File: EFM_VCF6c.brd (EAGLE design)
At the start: 100 x 80.6 mm, 69 parts, among them IC1 LM13700N, Q1 2N3904, Q2 2N3904, Q3 2N3906, Q4 2N3904, Q5 2N3906, U1 POWER

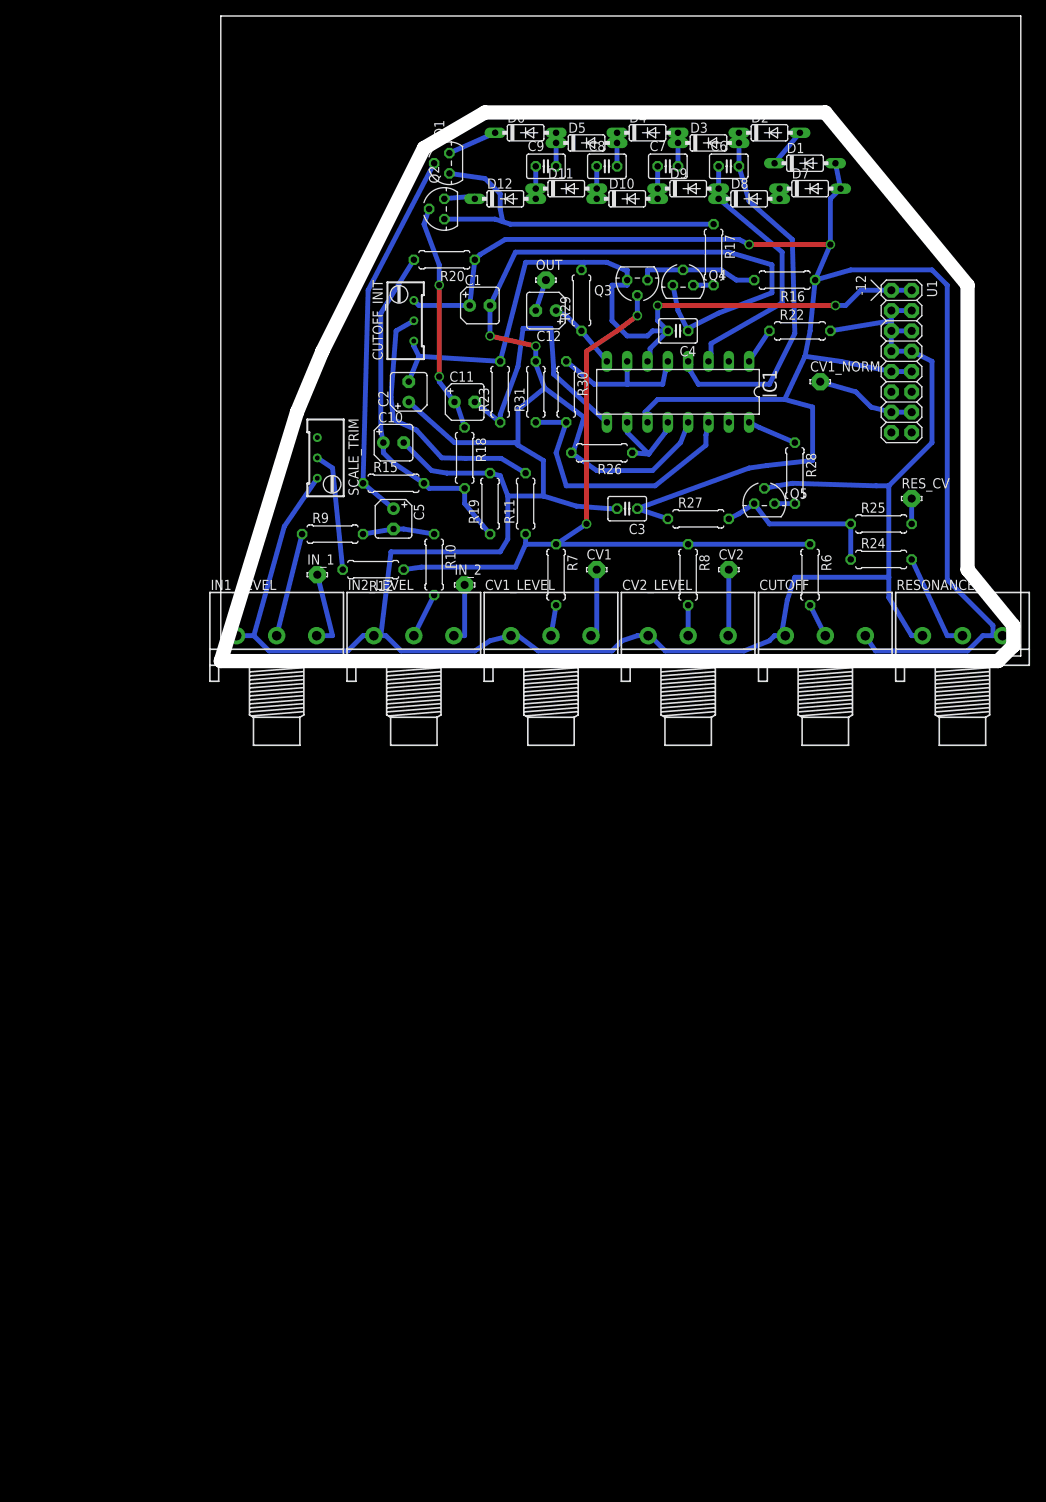
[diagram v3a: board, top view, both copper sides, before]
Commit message: updated power and pots and better diodes
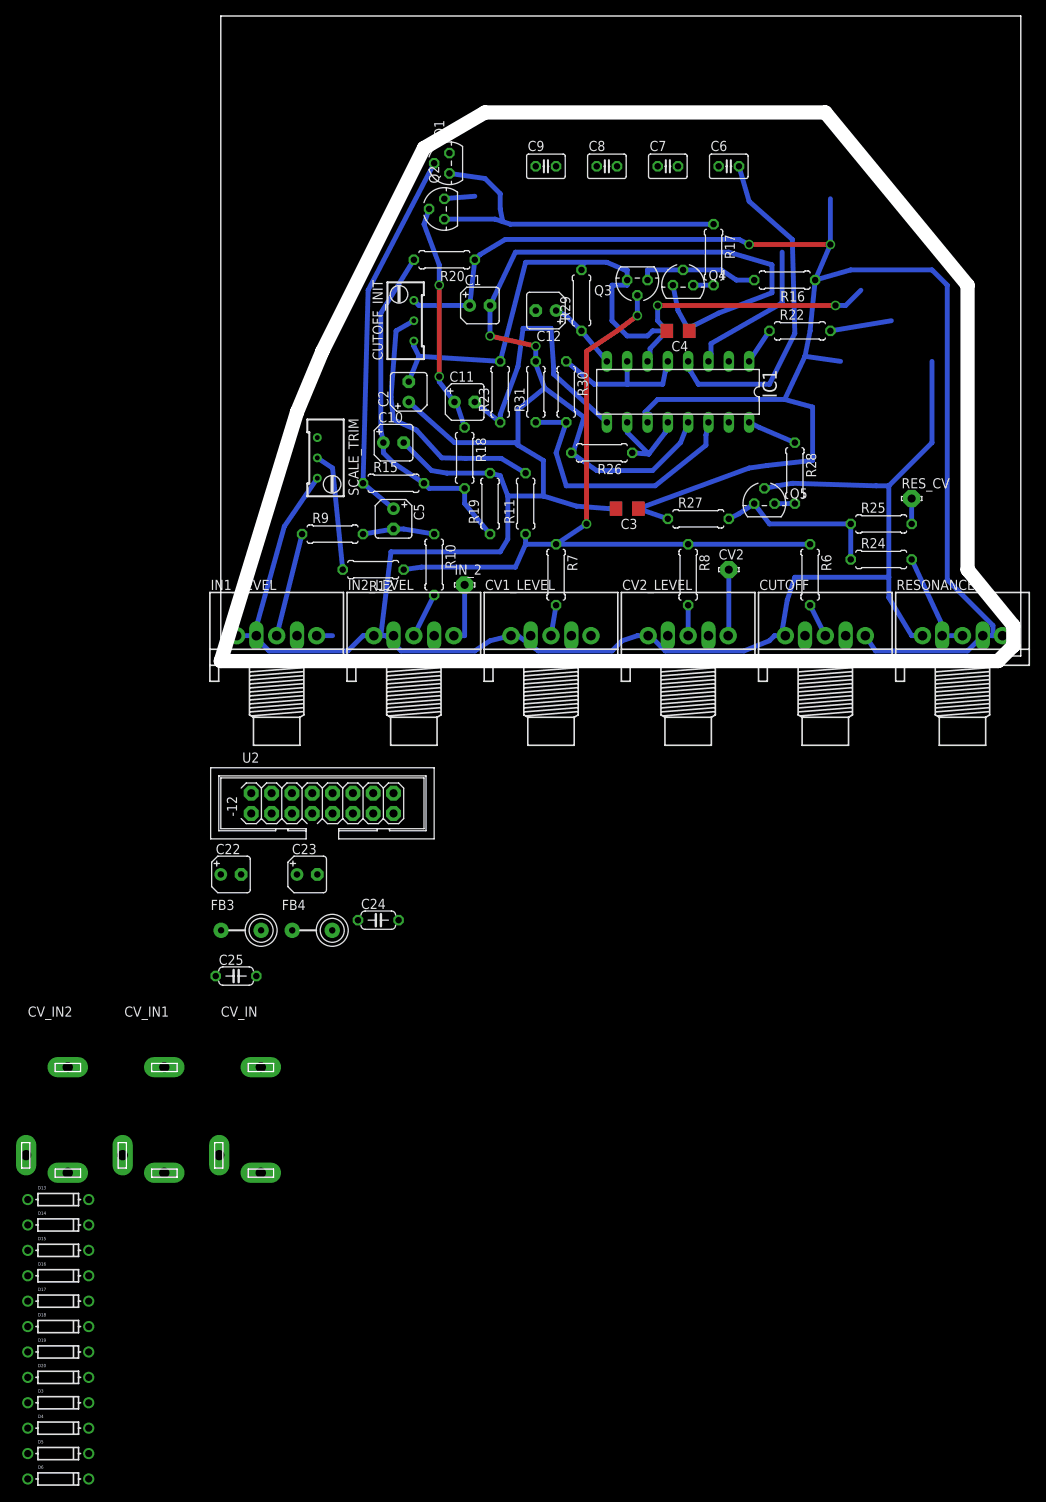
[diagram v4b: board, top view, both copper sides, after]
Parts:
- removed CV1, CV1_NORM, IN_1, OUT: LSP10, solpad:LSP10
- removed D1, D10, D11, D12, D2, D7, D8, D9: 1N4148DO35-7, diode:DO35-7
- removed U1: POWER, eurorack:POWER_16
- added C22, C23: 10u, rcl:B45181A
- added C24, C25: 100n, rcl:C050-024X044
- added CV_IN, CV_IN1, CV_IN2: AUDIO-JACKITEAD, erthenvar:JACK-90DEG-ITEAD
- added D13, D14, D15, D16, D17, D18, D19, D20: (no value), adafruit:DO-1N4148
- added FB3, FB4: FB, adafruit:FB
- added U2: POWER, eurorack:POWER_16
- C3, C4: device rcl:C025-030X050 -> rcl:C1206
- D3, D4, D5, D6: value 1N4148DO35-7 -> (none); device diode:DO35-7 -> adafruit:DO-1N4148
- moved D6 178.1 mm to (-20.3, -102.9)
- moved D4 177.9 mm to (-20.3, -96.5)
- moved D3 177.2 mm to (-20.3, -93.3)
- moved D5 176.6 mm to (-20.3, -99.7)
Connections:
- removed net N$55: CV1_NORM.MP, U1.13, U1.14
- new net +12V: C22.+, C24.1, FB3.P$2
- new net N$39: CV_IN.P$2, U2.13, U2.14
- new net N$41: FB3.P$1, U2.10, U2.9
- new net N$68: FB4.P$1, U2.1, U2.2
- net -12V: now also C23.-, C25.2, FB4.P$2; no longer U1.1, U1.2
- net GND: now also C22.-, C23.+, C24.2, C25.1, CUTOFF.4, CV1_LEVEL.4, CV2_LEVEL.4, CV_IN.P$1, CV_IN1.P$1, CV_IN2.P$1, IN1_LEVEL.4, IN2_LEVEL.4, RESONANCE.4, U2.3, U2.4, U2.5, U2.6, U2.7, U2.8; no longer U1.3, U1.4, U1.5, U1.6, U1.7, U1.8
- net N$12: now also D16.A, D4.C; no longer D8.C, D9.A
- net N$13: now also D13.A, D16.C; no longer D10.A, D9.C
- net N$14: now also D14.C, D20.A; no longer D4.C, D5.A
- net N$15: now also D13.C, D17.A; no longer D10.C, D11.A
- net N$17: now also D17.C, D18.A; no longer D11.C, D12.A
- net N$18: now also D19.A, D20.C; no longer D5.C, D6.A
- net N$19: now also D19.C; no longer D6.C
- net N$20: now also D18.C; no longer D12.C
- net N$21: now also D3.A, D5.C; no longer D1.C, D2.A
- net N$22: now also D4.A, D6.C; no longer D7.C, D8.A
- net N$29: now also D14.A, D15.C; no longer D3.C, D4.A
- net N$31: now also CV_IN2.P$3; no longer OUT.MP
- net N$34: now also IN2_LEVEL.6
- net N$38: now also CUTOFF.6, D5.A, D6.A, RESONANCE.6; no longer D1.A, D7.A, U1.10, U1.9
- net N$54: now also CV2_LEVEL.6
- net N$58: now also CV_IN1.P$3, IN1_LEVEL.6; no longer IN_1.MP
- net N$59: now also CV1_LEVEL.6, CV_IN.P$3; no longer CV1.MP
- net N$9: now also D15.A, D3.C; no longer D2.C, D3.A
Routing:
- net GND: track 393.2 -> 377.6 mm
- net N$12: track 33.3 -> 18.9 mm
- net N$38: track 242.7 -> 228.4 mm
- net N$55: track 12.5 -> 0.00 mm
- net N$59: track 8.97 -> 0.72 mm
- net N$58: track 9.84 -> 1.99 mm
- net -12V: track 99.7 -> 93.1 mm
- net N$19: track 6.25 -> 0.00 mm
- net N$21: track 4.96 -> 0.00 mm
- net N$9: track 46.9 -> 42.8 mm
- net N$29: track 4.19 -> 0.00 mm
- net N$18: track 4.19 -> 0.00 mm
- net N$14: track 4.19 -> 0.00 mm
- net N$17: track 4.06 -> 0.00 mm
- net N$15: track 4.06 -> 0.00 mm
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
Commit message: routed and labels adjusted
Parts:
- removed C1, C2: 10uF, rcl:B45181A
- removed CV1_LEVEL, CV2_LEVEL, IN1_LEVEL, IN2_LEVEL: 100k, pot:3RP/1610N
- removed CV_IN1, CV_IN2: AUDIO-JACKITEAD, erthenvar:JACK-90DEG-ITEAD
- added CV1_LEV, CV2_LEV, IN1_LEV, IN2_LEV: 100k, bourns_ptd:PTD901
- added IN1, OUT: AUDIO-JACKITEAD, erthenvar:JACK-90DEG-ITEAD
- C3, C4, C6, C7, C8, C9: value 0.1uF -> 100n
- CUTOFF, RESONANCE: device pot:3RP/1610N -> bourns_ptd:PTD901
- moved D6 168.1 mm to (69.2, 39.4)
- moved D4 167.5 mm to (69.2, 45.1), turned to 180 degrees
- moved D5 167.0 mm to (69.2, 41.3)
- moved D3 163.3 mm to (69.2, 43.2), turned to 180 degrees
- moved D16 146.0 mm to (59.1, 45.1), turned to 180 degrees
- moved D20 142.9 mm to (40.0, 39.4), turned to 180 degrees
- moved D17 139.5 mm to (40.0, 45.1), turned to 180 degrees
- moved D15 138.6 mm to (59.1, 39.4), turned to 180 degrees
- moved D19 138.4 mm to (31.8, 41.3), turned to 90 degrees
- moved D18 136.2 mm to (33.7, 41.3), turned to 270 degrees
- moved D13 132.9 mm to (49.5, 45.1), turned to 180 degrees
- moved D14 130.7 mm to (49.5, 39.4), turned to 180 degrees
- moved FB3 111.4 mm to (81.9, 43.8), turned to 180 degrees
- moved C25 107.0 mm to (81.9, 31.1), turned to 180 degrees
- moved C22 102.6 mm to (81.9, 36.2)
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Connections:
- net -12V: no longer C2.-
- net GND: now also CV1_LEV.1, CV2_LEV.1, IN1.P$1, IN1_LEV.1, IN2_LEV.1, OUT.P$1; no longer C1.-, C2.+, CUTOFF.4, CV1_LEVEL.1, CV1_LEVEL.4, CV2_LEVEL.1, CV2_LEVEL.4, CV_IN1.P$1, CV_IN2.P$1, IN1_LEVEL.1, IN1_LEVEL.4, IN2_LEVEL.1, IN2_LEVEL.4, RESONANCE.4
- net N$10: now also CV2_LEV.2; no longer CV2_LEVEL.2
- net N$31: now also OUT.P$3; no longer CV_IN2.P$3
- net N$34: now also IN2_LEV.3; no longer IN2_LEVEL.3, IN2_LEVEL.6
- net N$38: no longer C1.+, CUTOFF.6, RESONANCE.6
- net N$5: now also IN2_LEV.2; no longer IN2_LEVEL.2
- net N$53: now also CV1_LEV.2; no longer CV1_LEVEL.2
- net N$54: now also CV2_LEV.3; no longer CV2_LEVEL.3, CV2_LEVEL.6
- net N$57: now also IN1_LEV.2; no longer IN1_LEVEL.2
- net N$58: now also IN1.P$3, IN1_LEV.3; no longer CV_IN1.P$3, IN1_LEVEL.3, IN1_LEVEL.6
- net N$59: now also CV1_LEV.3; no longer CV1_LEVEL.3, CV1_LEVEL.6
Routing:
- net N$3: track 2.54 -> 134.0 mm, vias 0 -> 1
- net N$6: track 9.00 -> 100.3 mm, vias 0 -> 1
- net N$39: track 0.00 -> 90.5 mm, vias 0 -> 1
- net N$58: track 1.99 -> 78.3 mm
- net N$59: track 0.72 -> 74.6 mm, vias 0 -> 1
- net N$38: track 228.4 -> 159.4 mm, vias 2 -> 1
- net N$16: track 90.4 -> 136.8 mm
- net N$31: track 0.00 -> 44.7 mm
- net GND: track 377.6 -> 337.8 mm, vias 2 -> 1
- net N$4: track 44.5 -> 8.67 mm
- net N$27: track 32.6 -> 7.56 mm
- net N$25: track 43.9 -> 20.4 mm
- net N$26: track 28.7 -> 46.9 mm, vias 2 -> 1
- net N$41: track 0.00 -> 15.4 mm
- net N$35: track 34.5 -> 19.2 mm
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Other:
- board size 100 x 80.6 mm -> 98.1 x 47.6 mm
